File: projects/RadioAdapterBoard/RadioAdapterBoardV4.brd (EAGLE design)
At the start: 20.5 x 45.5 mm, 33 parts

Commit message: Radio Adapter Board PCB Ready
Also, minor edits to 0805 package, L3255M package, and job
sfe-ger274x.cam
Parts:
- C14, C15, C16, C17, C18, C19, C20, C21, C22, C23, R10, R11, R12, R5, R6, R7, R8, R9: device CNTRL_BOARD:0805 -> BrownSpaceEngineering:0805
- moved V5 2.76 mm to (-17.8, 39.8)
- moved C16 1.27 mm to (-10.3, 25.7)
- moved R4 1.27 mm to (-3.84, 11.1)
- moved R3 1.25 mm to (-1.94, 11.1)
- moved R5 1.03 mm to (-16.4, 32.1)
- moved R7 1.03 mm to (-9.95, 32.1)
- moved R6 1.00 mm to (-13.2, 32.1)
- moved C17 0.79 mm to (-9.95, 30.3)
- moved C23 0.79 mm to (-16.4, 30.3)
- moved R12 0.75 mm to (-13.2, 30.3)
- moved L2 0.56 mm to (-9.41, 9.30)
- moved R10 0.56 mm to (-9.95, 28.6)
- moved C21 0.50 mm to (-8.92, 11.9)
- moved R9 0.50 mm to (-13.2, 28.6)
- moved R11 0.35 mm to (-8.28, 21.2)
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- renumbered PWR_ON to PWR
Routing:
- net VIN: track 39.2 -> 43.1 mm
- net 3V6-REF: track 15.0 -> 16.5 mm
- net N$26: track 7.27 -> 8.55 mm
- net 3V6: track 30.6 -> 29.4 mm
- net 3V6-EN: track 31.3 -> 30.1 mm
- net OVP: track 14.2 -> 15.3 mm
- net 3V6-SNS: track 34.3 -> 33.3 mm
- net FB: track 13.9 -> 14.9 mm
- net N$29: track 2.70 -> 3.49 mm
- net N$28: track 6.90 -> 7.50 mm
- net P3: track 24.3 -> 24.8 mm
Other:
- board text added: "EquiSat Radio Adapter Board V4.0 December 2016 Caelan Ritter Ryan Izant"
- board text added: "Side +Y"
- board text added: "Side -Y"
- board text removed: "+Y Side"
- board text removed: "-Y Side"
- board text removed: "EquiSat Radio Adapter Board V4.0 December 2016 Ryan Izant Caelan Ritter"

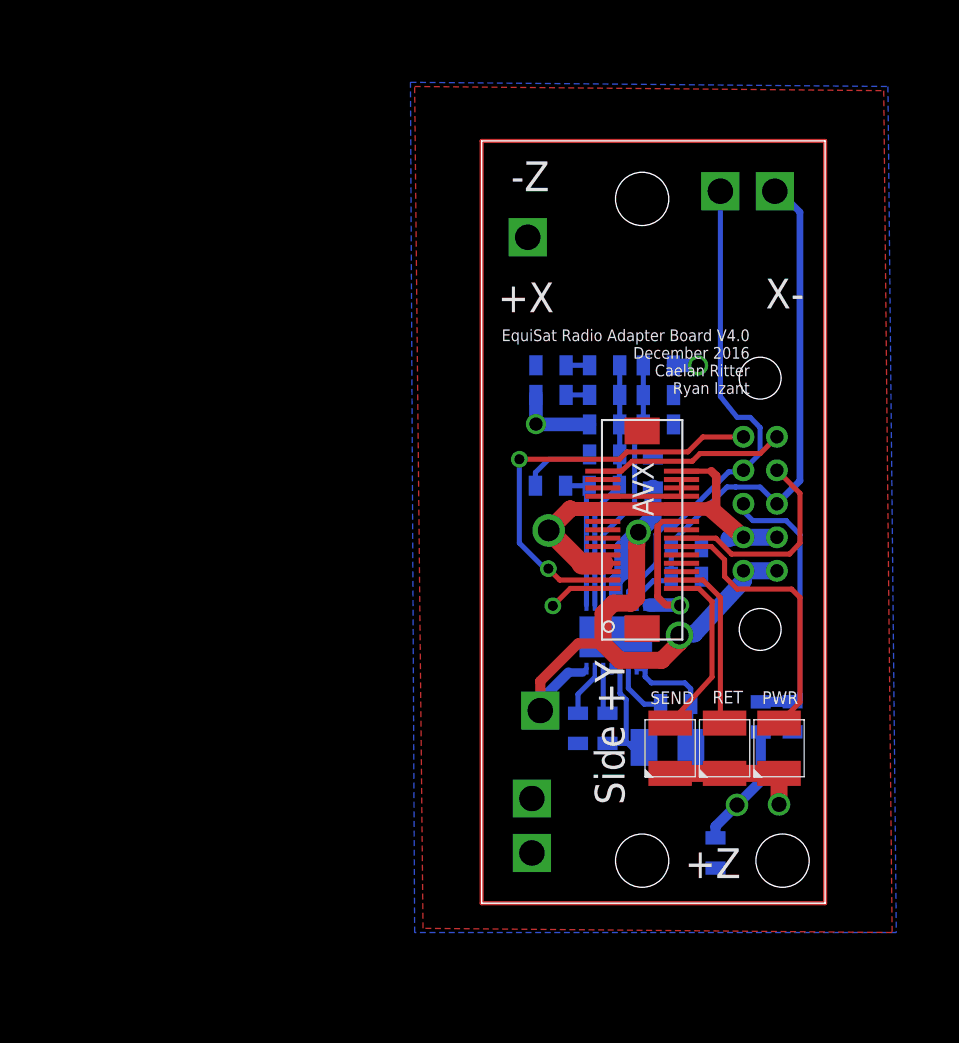
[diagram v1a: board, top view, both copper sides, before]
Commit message: Updates to Radio Adapter Board, Driver Board, Flash Panel. Somebody forgot to commit for a whole week or so....
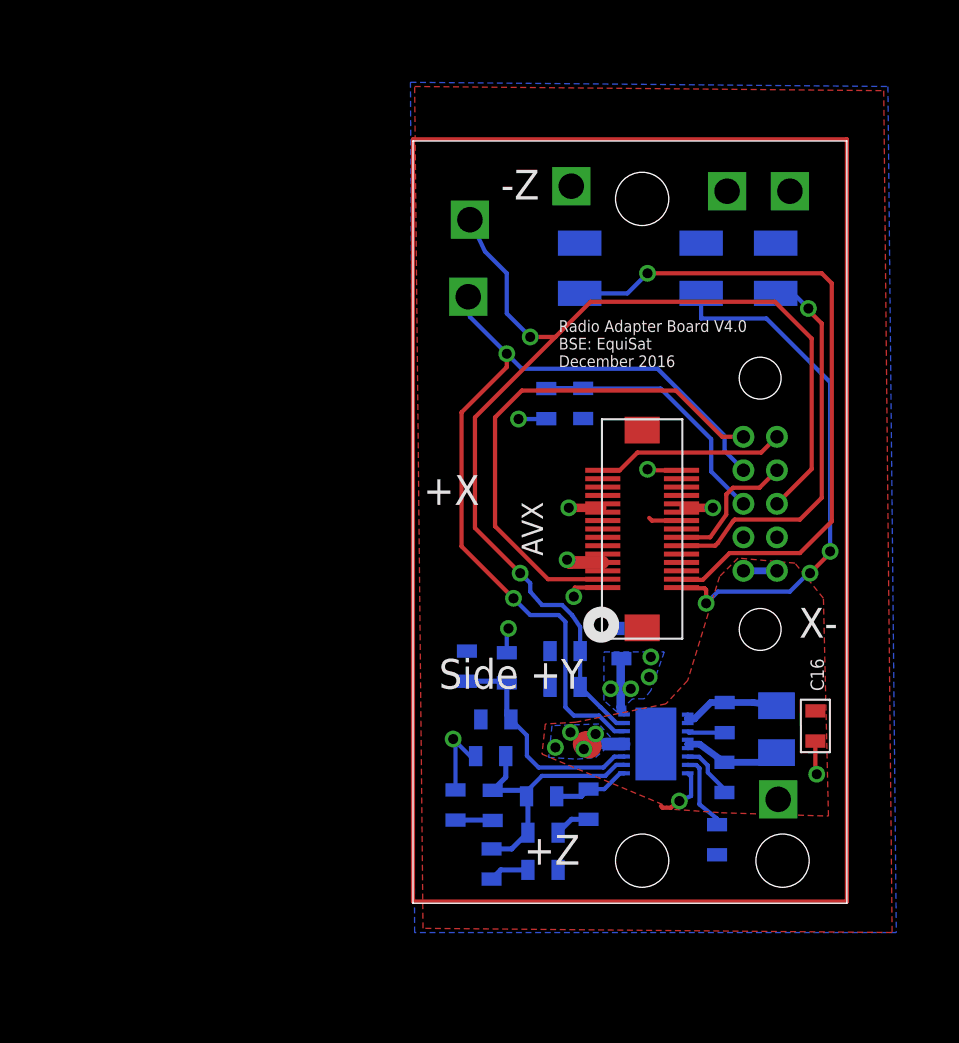
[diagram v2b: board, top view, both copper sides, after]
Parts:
- moved V3 42.4 mm to (-2.10, 42.5), turned to 270 degrees
- moved V4 38.1 mm to (-5.85, 42.5), turned to 270 degrees
- moved R6 30.5 mm to (-19.9, 2.34), turned to 270 degrees
- moved R5 30.1 mm to (-16.8, 1.99), turned to 180 degrees
- moved RET 28.5 mm to (-14.7, 37.1), flipped to the bottom, turned to 180 degrees
- moved SEND 27.2 mm to (-7.40, 37.1), flipped to the bottom, turned to 180 degrees
- moved PWR 27.2 mm to (-2.95, 37.1), flipped to the bottom, turned to 180 degrees
- moved R12 25.4 mm to (-19.8, 5.84), turned to 270 degrees
- moved C23 25.1 mm to (-22.1, 5.86), turned to 270 degrees
- moved R8 22.9 mm to (-16.8, 4.21), turned to 0 degrees
- moved R4 22.7 mm to (-16.6, 29.8)
- moved R3 22.5 mm to (-14.4, 29.8)
- moved C17 21.7 mm to (-19.6, 11.0), turned to 0 degrees
- moved R9 20.9 mm to (-20.0, 8.78)
- moved R7 20.2 mm to (-19.0, 14.1), turned to 90 degrees
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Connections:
- net 3V6: now also AVX.P18, AVX.P23, AVX.P24, AVX.P25, AVX.P26, AVX.P27, AVX.P28; no longer AVX.18, AVX.23, AVX.24, AVX.25, AVX.26, AVX.27, AVX.28
- net GND: now also AVX.P1, AVX.P19, AVX.P20, AVX.P21, AVX.P22, AVX.P30, AVX.P5, AVX.P7, AVX.P9; no longer AVX.1, AVX.19, AVX.20, AVX.21, AVX.22, AVX.30, AVX.5, AVX.7, AVX.9
- net P12: now also AVX.P12; no longer AVX.12
- net P14: now also AVX.P14; no longer AVX.14
- net P2: now also AVX.P2; no longer AVX.2
- net P29: now also AVX.P29; no longer AVX.29
- net P3: now also AVX.P3; no longer AVX.3
- net P4: now also AVX.P4; no longer AVX.4
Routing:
- net VIN: track 43.1 -> 7.33 mm, vias 2 -> 5
- net 3V6-SNS: track 33.3 -> 67.2 mm, vias 0 -> 2
- net P4: track 10.4 -> 40.4 mm, vias 0 -> 1
- net GND: track 40.3 -> 14.7 mm, vias 3 -> 6
- net 3V6-EN: track 30.1 -> 51.7 mm, vias 0 -> 2
- net P2: track 10.4 -> 31.9 mm, vias 0 -> 3
- net 3V6: track 29.4 -> 13.9 mm, vias 4 -> 7
- net N$1: track 132.0 -> 142.8 mm
- net P12: track 16.9 -> 23.7 mm, vias 0 -> 1
- net P3: track 24.8 -> 30.9 mm, vias 2 -> 0
- net P14: track 12.7 -> 8.20 mm
- net COMP: track 8.60 -> 4.59 mm
- net N$4: track 4.60 -> 2.15 mm
- net N$26: track 8.55 -> 6.39 mm
- net OVP: track 15.3 -> 13.6 mm
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- added copper zone on layer 16, net 3V6
- added copper zone on layer 1, net VIN
- added copper zone on layer 16, net VIN
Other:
- board size 20.5 x 45.5 mm -> 25.9 x 45.5 mm
- board text added: "Radio Adapter Board V4.0 BSE: EquiSat December 2016"
- board text removed: "EquiSat Radio Adapter Board V4.0 December 2016 Caelan Ritter Ryan Izant"
